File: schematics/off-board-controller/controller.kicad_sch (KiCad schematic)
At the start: 18 parts, among them SW1 SW_Push, SW2 SW_Push, SW3 SW_Push, SW4 SW_SPDT_MSM, U1 NUCLEO144-F446ZE, U2 RFM98W-433S2, U3 CA56-12EWA

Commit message: off-board: created schematic
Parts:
- removed +3V: Battery, symbol Device:Battery
- removed Joystick: ~, symbol New_Library:2DirJoystick
- removed SW2: SW_Push, symbol Switch:SW_Push
- removed SW4: SW_SPDT_MSM, symbol Switch:SW_SPDT_MSM
- added +3V1: Battery, symbol Device:Battery
- added Joystick1: ~, symbol New_Library:2DirJoystick
- added SW2: SW_SPDT_MSM, symbol Switch:SW_SPDT_MSM
- added SW4: SW_Push, symbol Switch:SW_Push
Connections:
- net at U3.1 (e): now also R3.1; no longer R5.1
- net at R5.2: now also U1.69 (STLINK_RX/PD9); no longer U1.115 (PD12)
- net at U3.10 (f): now also R7.1; no longer R6.1
- net at U1.113 (PD13): now also R7.2; no longer R6.2
- net at U3.4 (c): now also R2.1; no longer R3.1
- net at U1.137 (PD10): now also R2.2; no longer R3.2
- net at R4.1: now also U3.5 (g); no longer U3.2 (d)
- net at R4.2: now also U1.118 (PD14); no longer U1.117 (PD11)
- net at U1.35 (PC2): now also SW1.1; no longer SW3.1
- net at SW1.2, SW3.2, U1.104 (AGND)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: now also +3V1.2 (-), Joystick1.3 (GND), SW4.2
- net at U1.36 (ETH_MDC/PC1): now also SW3.1
- net at U3.7 (b): now also R5.1; no longer R2.1
- net at U1.5 (VDD), U1.79 (AVDD), U2.13 (3.3V): now also +3V1.1 (+), Joystick1.2 (PWR), SW2.2 (3)
- net at U1.38 (PC0): now also SW4.1; no longer SW1.1
- net at U1.103 (SWO/PB3): now also SW2.3 (4)
- net at U1.34 (PB0): now also Joystick1.0 (VRx)
- net at U1.94 (PB2): now also SW2.1
- net at U1.96 (PB1): now also Joystick1.1 (VRy)
- new net: R6.1, U3.2 (d)
- new net: R6.2, U1.117 (PD11)
- new net: R3.2, U1.115 (PD12)
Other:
- added sheet io (io.kicad_sch)
- added sheet mcu (mcu.kicad_sch)
- added sheet power (power.kicad_sch)
- added sheet radio (radio.kicad_sch)
- title: Off-Board Controller -> Off-board Controller

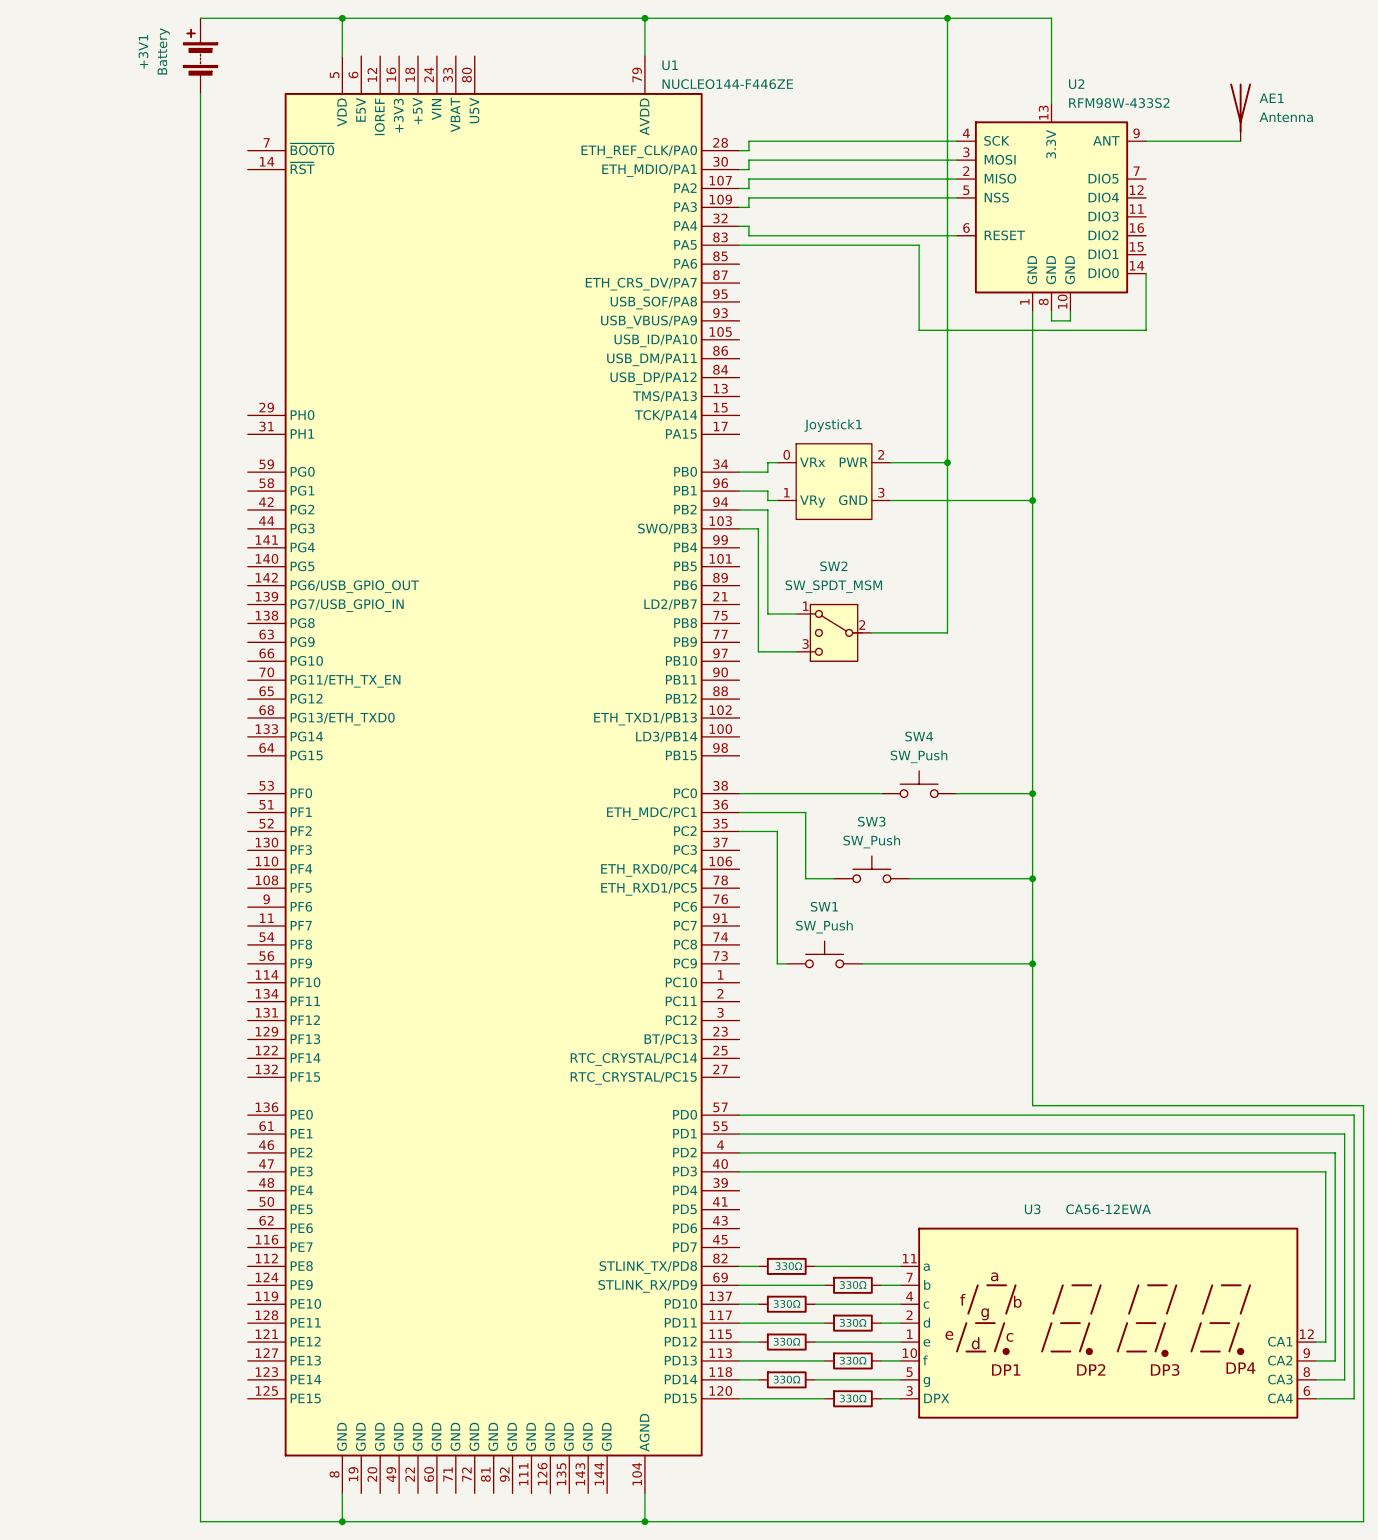
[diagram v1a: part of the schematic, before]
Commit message: finished footprints, schematic, and started layout
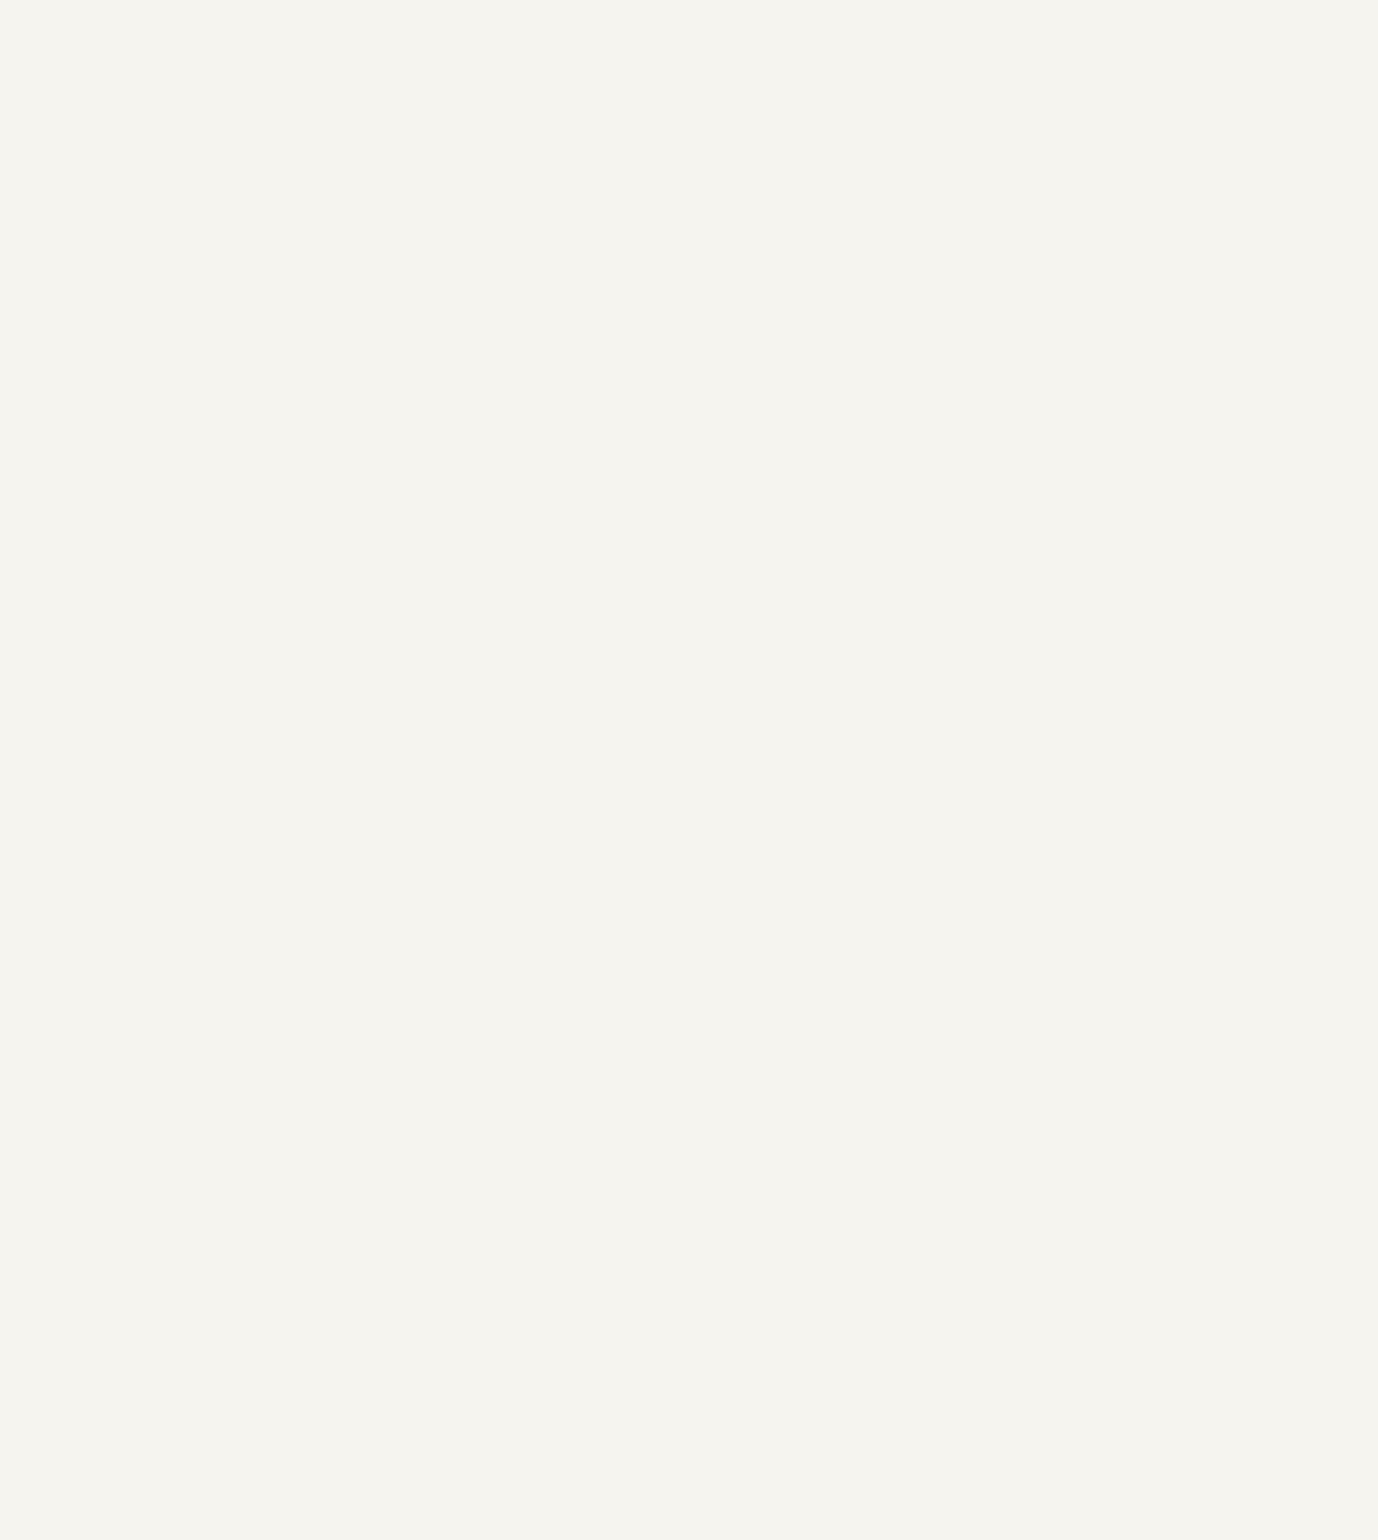
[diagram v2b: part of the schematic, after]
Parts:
- removed +3V1: Battery, symbol Device:Battery
- removed AE1: Antenna, symbol Device:Antenna
- removed Joystick1: ~, symbol New_Library:2DirJoystick
- removed R1, R2, R3, R4, R5, R6, R7, R8: 330Ω, symbol Device:R
- removed SW1, SW3, SW4: SW_Push, symbol Switch:SW_Push
- removed SW2: SW_SPDT_MSM, symbol Switch:SW_SPDT_MSM
- removed U1: NUCLEO144-F446ZE, Module:ST_Morpho_Connector_144_STLink, symbol MCU_Module:NUCLEO144-F446ZE
- removed U2: RFM98W-433S2, symbol RF_Module:RFM98W-433S2
- removed U3: CA56-12EWA, Display_7Segment:CA56-12EWA, symbol Display_Character:CA56-12EWA
